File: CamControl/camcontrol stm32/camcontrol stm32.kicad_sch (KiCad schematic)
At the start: 42 parts, among them J1 Power 1, J2 USB_B_Micro, J3 Power 1, J4 Power 1, J5 Power 1, J6 Conn_01x02, J7 Power 1, Q1 AO3401A, Q3 AO3401A, U1 BGS12WN6E6327, U2 BALFHB-WL-02D3, U3 STM32WLE4CCUx, U4 XC6206P332MR, U5 TPS25970LRPWR, U6 TPS25970LRPWR, Y1 32MHz

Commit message: work
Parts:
- removed J2: USB_B_Micro, easyeda2kicad2:MICRO-USB-SMD_U254-051T-4BHJ25-F2S, symbol Connector:USB_B_Micro
- removed J5: Power 1, Connector_Molex:Molex_PicoBlade_53048-0210_1x02_P1.25mm_Horizontal, symbol Connector:Screw_Terminal_01x02
- added C17: 100n, Capacitor_SMD:C_0402_1005Metric, symbol Device:C_Small
- added D2: LED, LED_SMD:LED_0603_1608Metric, symbol Device:LED
- added H1, H2: MountingHole_Pad, MountingHole:MountingHole_2.2mm_M2_DIN965_Pad, symbol Mechanical:MountingHole_Pad
- added J5: Conn_01x06, Connector_PinHeader_1.27mm:PinHeader_1x06_P1.27mm_Vertical, symbol Connector_Generic:Conn_01x06
- added J8: DNP, Connector_PinHeader_2.54mm:PinHeader_1x05_P2.54mm_Vertical, symbol Connector:Conn_01x05_Pin
- added R23, R8: 15k, Resistor_SMD:R_0402_1005Metric, symbol Device:R_Small
- added R24, R9: 51k, Resistor_SMD:R_0402_1005Metric, symbol Device:R_Small
- added R3, R5: 20m, Resistor_SMD:R_0402_1005Metric, symbol Device:R_Small
- added R7: 1k, Resistor_SMD:R_0402_1005Metric, symbol Device:R_Small
- added U7: INA2180, Package_SON:WSON-8-1EP_2x2mm_P0.5mm_EP0.9x1.6mm, symbol .kicad_sym:INA2180
- C15: now not fitted
- C2, C3: footprint Capacitor_SMD:C_0402_1005Metric -> Capacitor_SMD:C_0201_0603Metric
- J1, J3, J4, J7: footprint Connector_Molex:Molex_PicoBlade_53048-0210_1x02_P1.25mm_Horizontal -> Connector_Molex:Molex_PicoBlade_53261-0271_1x02-1MP_P1.25mm_Horizontal
- L1: footprint Inductor_SMD:L_0201_0603Metric -> Inductor_SMD:L_0402_1005Metric
- gave numbers to parts that had none: 1
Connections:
- net PRW1 EN is gone; now on net PRWA EN: U5.1 (EN/UVLO)
- net PWR2 EN is gone; now on net PWRB EN: U6.1 (EN/UVLO)
- net +12V: now also R23.1
- net +12VA: now also R8.1
- net +3V3: now also U1.4 (VDD), C17.1, U7.8 (VS); no longer U3.29 (VDDRF1V55)
- net GND: now also AE1.2 (Shield), J3.1 (Pin_1), J7.1 (Pin_1), U1.2 (GND), C17.2, H1.1, H2.1, J5.3 (Pin_3), J5.6 (Pin_6), J8.4 (Pin_4), J8.5 (Pin_5), R24.2, R7.2, R9.2, U7.4 (GND); no longer J3.2 (Pin_2), J7.2 (Pin_2)
- net PWR A: now also J7.2 (Pin_2), R5.2, U7.2 (IN-1); no longer J7.1 (Pin_1), U5.6 (OUT), U6.6 (OUT)
- net PWR B: now also J3.2 (Pin_2), R3.2, U7.6 (IN-2); no longer J3.1 (Pin_1)
- net VBUS: now also J8.3 (Pin_3)
- net VFBSMPS: now also U3.29 (VDDRF1V55), U3.45 (VFBSMPS)
- net CAM1 TX: now reaches U3.10 (PA3)
- net CAM1 TX: now also J5.2 (Pin_2), J8.2 (Pin_2)
- net BATT SENSE A: now reaches U3.12 (PA4)
- net BATT SENSE A: now also R8.2, R9.1
- net PWRB EN: now reaches U3.13 (PA5)
- net BATT SENSE B: now reaches U3.14 (PA6)
- net BATT SENSE B: now also R23.2, R24.1
- net PRWA EN: now reaches U3.2 (PB4)
- net LED INDICATION: now reaches U3.30 (PB0)
- net LED INDICATION: now also D2.2 (A)
- net CURRENT SENSE B: now reaches U3.34 (PA11)
- net CURRENT SENSE B: now also U7.7 (OUT2)
- net RF CTRL: now reaches U3.38 (PC13)
- net RF CTRL: now also U1.6 (CTRL)
- net CAM2 RX: now reaches U3.4 (PB6)
- net CAM2 RX: now also J5.4 (Pin_4)
- net CAM2 TX: now reaches U3.5 (PB7)
- net CAM2 TX: now also J5.5 (Pin_5)
- net CURRENT SENSE A: now reaches U3.7 (PA0)
- net CURRENT SENSE A: now also U7.1 (OUT1)
- net CAM1 RX: now reaches U3.9 (PA2)
- net CAM1 RX: now also J5.1 (Pin_1), J8.1 (Pin_1)
- new net: D2.1 (K), R7.1
- new net PWR A SENS: R5.1, U5.6 (OUT), U7.3 (IN+1)
- new net PWR B SENS: R3.1, U6.6 (OUT), U7.5 (IN+2)
- no-connect marks 10 -> 27
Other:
- note added: "CURRENT MONITER"
- note added: "DATASHEET"
- note added: "FROM BRIAN"
- note added: "FROM: FOO"
- note added: "MCU"
- note added: "SWITCHES"
- moved on the sheet: C1, C12, C18, J1, J3, J4, J7, R2, R6, U5, U6

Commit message: final version?
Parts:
- removed D4: D_Schottky, Diode_SMD:D_SOD-323F, symbol Device:D_Schottky
- removed H1, H2: MountingHole_Pad, MountingHole:MountingHole_2.2mm_M2_DIN965_Pad, symbol Mechanical:MountingHole_Pad
- removed J8: DNP, Connector_PinHeader_2.54mm:PinHeader_1x05_P2.54mm_Vertical, symbol Connector:Conn_01x05_Pin
- removed Q3: AO3401A, Package_TO_SOT_SMD:SOT-23, symbol Transistor_FET:AO3401A
- removed U4: XC6206P332MR, Package_TO_SOT_SMD:SOT-23-3, symbol .kicad_sym:XC6206P332MR
- added D3: D_Zener, Diode_SMD:D_SOD-523F, symbol Device:D_Zener
- added H1, H2: MountingHole, MountingHole:MountingHole_2.2mm_M2_DIN965, symbol Mechanical:MountingHole
- added J2: Conn_01x04, Connector_PinHeader_2.54mm:PinHeader_1x04_P2.54mm_Vertical, symbol Connector_Generic:Conn_01x04
- added R10: 51k, Resistor_SMD:R_0402_1005Metric, symbol Device:R_Small
- added U4: DS8242, :SOT-23-3_L2.9-W1.6-P1.90-LS2.8-BR, symbol .kicad_sym:DS8242
- J1, J3, J4, J7: footprint Connector_Molex:Molex_PicoBlade_53261-0271_1x02-1MP_P1.25mm_Horizontal -> Connector_Molex:Molex_PicoBlade_53048-0210_1x02_P1.25mm_Horizontal
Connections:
- net +3V3: now also J2.2 (Pin_2), U4.2 (Vout)
- net BATT SENSE A: now also U3.36 (PA13); no longer U3.12 (PA4)
- net BATT SENSE B: now also U3.12 (PA4); no longer U3.14 (PA6)
- net CAM1 RX: now also J2.4 (Pin_4)
- net CAM1 TX: now also J2.3 (Pin_3)
- net CURRENT SENSE B: now also U3.8 (PA1); no longer U3.34 (PA11)
- net GND: now also J2.1 (Pin_1), R10.2, U4.1 (GND); no longer Q1.1 (G)
- net LED INDICATION: now also U3.35 (PA12); no longer U3.30 (PB0)
- net at C5.1, Q1.2 (S): now also D3.1 (K), U4.3 (Vin)
- net at JP1.2 (C): now also Q1.3 (D)
- new net: D3.2 (A), Q1.1 (G), R10.1
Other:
- moved on the sheet: Q1

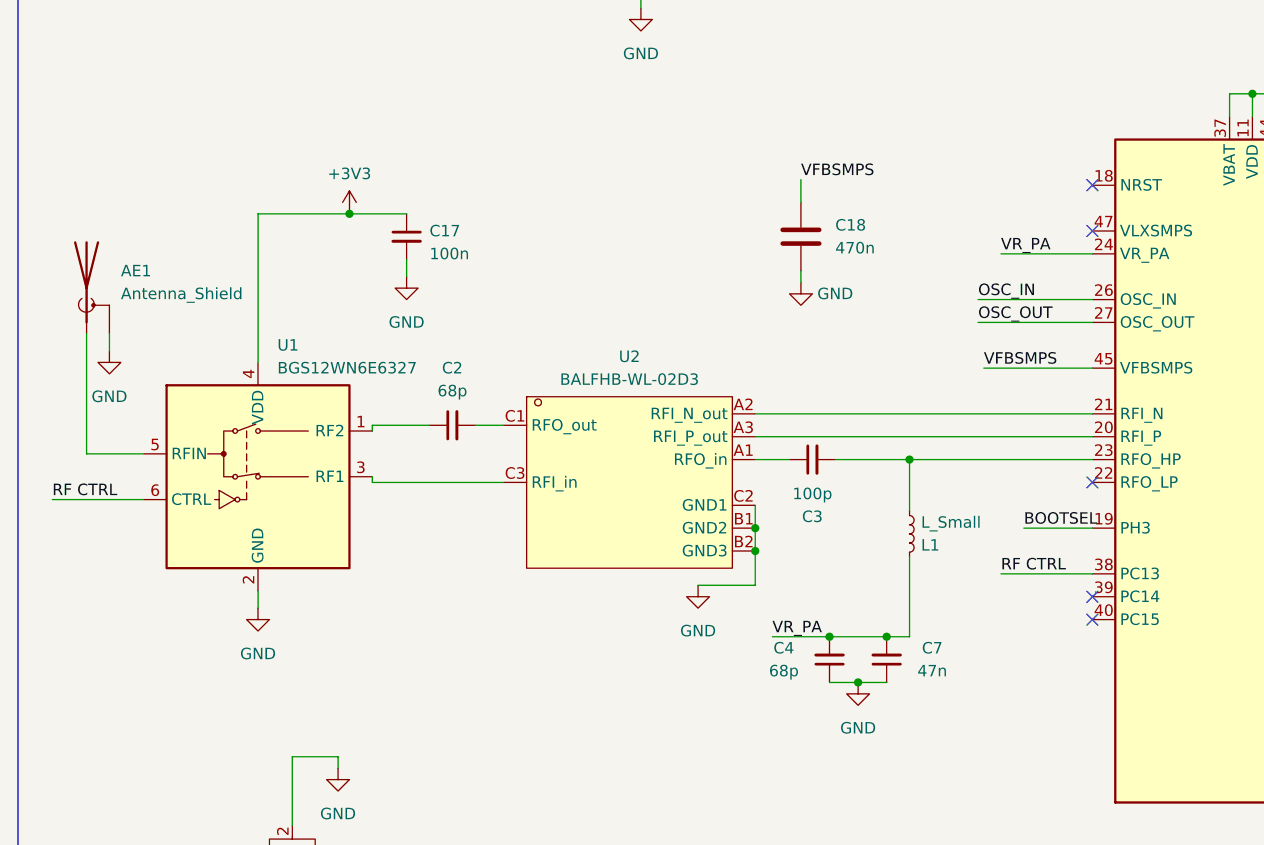
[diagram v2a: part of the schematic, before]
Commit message: rf rework and redrawing
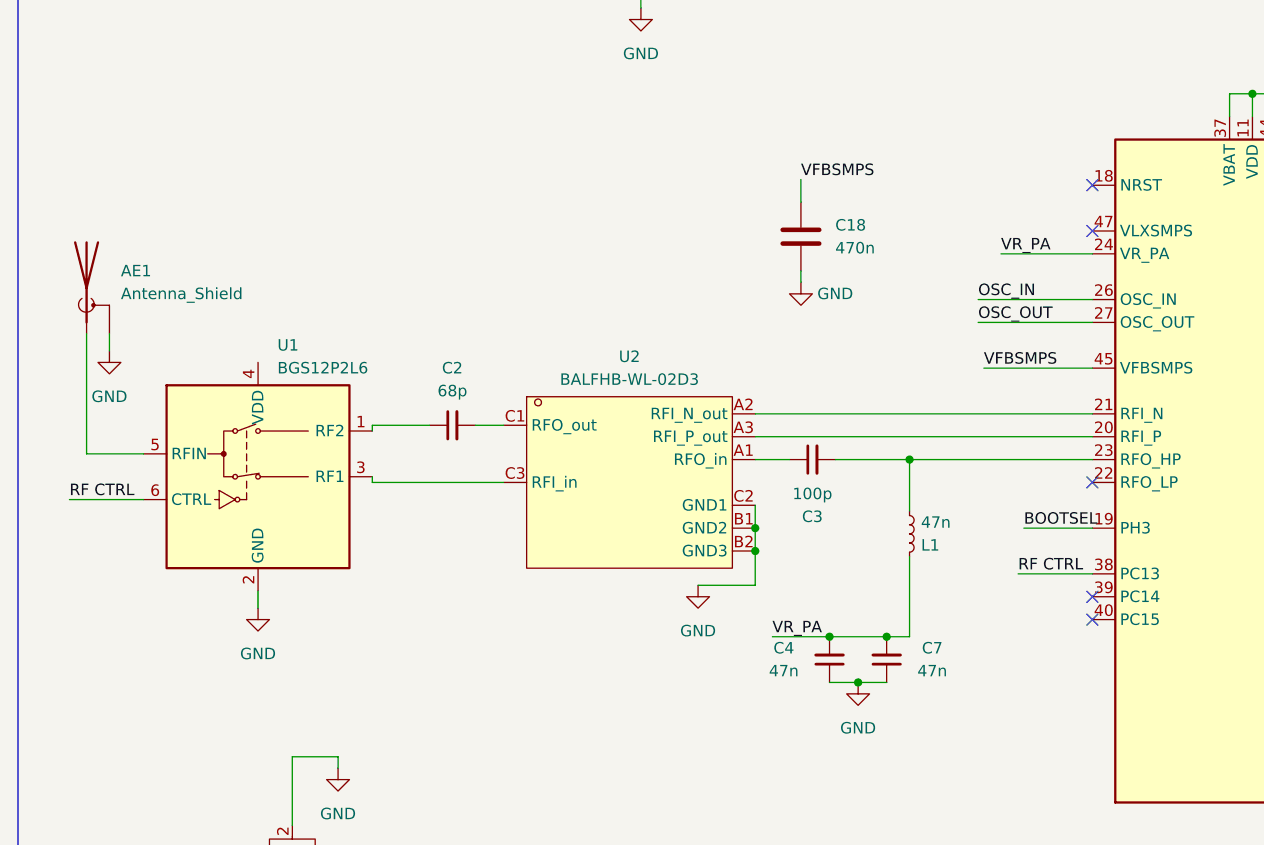
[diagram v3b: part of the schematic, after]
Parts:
- removed C17: 100n, Capacitor_SMD:C_0402_1005Metric, symbol Device:C_Small
- C18: LCSC Part (none) -> C47339
- C4: value 68p -> 47n
- D3: LCSC Part (none) -> C7420320
- L1: value L_Small -> 47n; LCSC Part (none) -> C22334
- R2, R6: LCSC Part (none) -> C25123
- R23, R8: LCSC Part (none) -> C25756
- R4: LCSC Part (none) -> C25779
- U1: value BGS12WN6E6327 -> BGS12P2L6
- U3: LCSC Part (none) -> C2888218
- Y1: LCSC Part (none) -> C383840
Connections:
- net +3V3: no longer U1.4 (VDD)

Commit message: update
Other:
- moved on the sheet: D1, R1
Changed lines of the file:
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@@
 	(rectangle
 		(start 227.965 175.26)
-		(end 283.845 285.115)
+		(end 283.845 284.48)
 		(stroke
 			(width 0)
@@
 	(wire
 		(pts
-			(xy 292.1 181.61) (xy 292.1 180.975)
+			(xy 299.72 186.69) (xy 299.72 186.055)
 		)
 		(stroke
@@
 	(wire
 		(pts
-			(xy 292.1 189.23) (xy 292.1 191.135)
+			(xy 299.72 194.31) (xy 299.72 196.215)
 		)
 		(stroke
@@
 	(wire
 		(pts
-			(xy 292.1 197.485) (xy 292.1 196.215)
+			(xy 299.72 202.565) (xy 299.72 201.295)
 		)
 		(stroke
@@
 	(symbol
 		(lib_id "Device:LED")
-		(at 292.1 185.42 90)
+		(at 299.72 190.5 90)
 		(unit 1)
 		(exclude_from_sim no)
@@
 		(fields_autoplaced yes)
 		(property "Reference" "D1"
-			(at 289.56 188.2776 90)
+			(at 297.18 193.3576 90)
 			(effects
 				(font
@@
 		)
 		(property "Value" "LED"
-			(at 289.56 185.7376 90)
+			(at 297.18 190.8176 90)
 			(effects
 				(font
@@
 		)
 		(property "Footprint" "LED_SMD:LED_0603_1608Metric"
-			(at 292.1 185.42 0)
+			(at 299.72 190.5 0)
 			(effects
 				(font
@@
 		)
 		(property "Datasheet" "~"
-			(at 292.1 185.42 0)
+			(at 299.72 190.5 0)
 			(effects
 				(font
@@
 		)
 		(property "Description" "Light emitting diode"
-			(at 292.1 185.42 0)
+			(at 299.72 190.5 0)
 			(effects
 				(font
@@
 		)
 		(property "LCSC Part" "C89811"
-			(at 292.1 185.42 90)
+			(at 299.72 190.5 90)
 			(effects
 				(font
@@
 		)
 		(property "Sim.Pins" "1=K 2=A"
-			(at 292.1 185.42 0)
+			(at 299.72 190.5 0)
 			(effects
 				(font
@@
 		)
 		(property "Part #" ""
-			(at 292.1 185.42 90)
+			(at 299.72 190.5 90)
 			(effects
 				(font
@@
 	(symbol
 		(lib_id "power:GND")
-		(at 292.1 197.485 0)
+		(at 299.72 202.565 0)
 		(unit 1)
 		(exclude_from_sim no)
@@
 		(fields_autoplaced yes)
 		(property "Reference" "#PWR013"
-			(at 292.1 203.835 0)
+			(at 299.72 208.915 0)
 			(effects
 				(font
@@
 		)
 		(property "Value" "GND"
-			(at 292.1 202.565 0)
+			(at 299.72 207.645 0)
 			(effects
 				(font
@@
 		)
 		(property "Footprint" ""
-			(at 292.1 197.485 0)
+			(at 299.72 202.565 0)
 			(effects
 				(font
@@
 		)
 		(property "Datasheet" ""
-			(at 292.1 197.485 0)
+			(at 299.72 202.565 0)
 			(effects
 				(font
@@
 		)
 		(property "Description" "Power symbol creates a global label with name \"GND\" , ground"
-			(at 292.1 197.485 0)
+			(at 299.72 202.565 0)
 			(effects
 				(font
@@
 	(symbol
 		(lib_id "power:+3V3")
-		(at 292.1 180.975 0)
+		(at 299.72 186.055 0)
 		(unit 1)
 		(exclude_from_sim no)
@@
 		(fields_autoplaced yes)
 		(property "Reference" "#PWR012"
-			(at 292.1 184.785 0)
+			(at 299.72 189.865 0)
 			(effects
 				(font
@@
 		)
 		(property "Value" "+3V3"
-			(at 292.1 177.165 0)
+			(at 299.72 182.245 0)
 			(effects
 				(font
@@
 		)
 		(property "Footprint" ""
-			(at 292.1 180.975 0)
+			(at 299.72 186.055 0)
 			(effects
 				(font
@@
 		)
 		(property "Datasheet" ""
-			(at 292.1 180.975 0)
+			(at 299.72 186.055 0)
 			(effects
 				(font
@@
 		)
 		(property "Description" "Power symbol creates a global label with name \"+3V3\""
-			(at 292.1 180.975 0)
+			(at 299.72 186.055 0)
 			(effects
 				(font
@@
 	(symbol
 		(lib_id "Device:R_Small")
-		(at 292.1 193.675 0)
+		(at 299.72 198.755 0)
 		(unit 1)
 		(exclude_from_sim no)
@@
 		(fields_autoplaced yes)
 		(property "Reference" "R1"
-			(at 290.195 194.31 0)
+			(at 297.815 199.39 0)
 			(effects
 				(font
@@
 		)
 		(property "Value" "1k"
-			(at 290.195 191.77 0)
+			(at 297.815 196.85 0)
 			(effects
 				(font
@@
 		)
 		(property "Footprint" "Resistor_SMD:R_0402_1005Metric"
-			(at 292.1 193.675 0)
+			(at 299.72 198.755 0)
 			(effects
 				(font
@@
 		)
 		(property "Datasheet" "~"
-			(at 292.1 193.675 0)
+			(at 299.72 198.755 0)
 			(effects
 				(font
@@
 		)
 		(property "Description" "Resistor, small symbol"
-			(at 292.1 193.675 0)
+			(at 299.72 198.755 0)
 			(effects
 				(font
@@
 		)
 		(property "LCSC Part" "C11702"
-			(at 292.1 193.675 0)
+			(at 299.72 198.755 0)
 			(effects
 				(font
@@
 		)
 		(property "LCSC_Part" ""
-			(at 292.1 193.675 0)
+			(at 299.72 198.755 0)
 			(effects
 				(font
@@
 		)
 		(property "Part #" ""
-			(at 292.1 193.675 0)
+			(at 299.72 198.755 0)
 			(effects
 				(font

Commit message: hopefully prod version
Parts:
- C2: LCSC Part (none) -> C14441
- C3: LCSC Part (none) -> C1546
- C4, C7: LCSC Part (none) -> C5142571
- R3, R5: value 20m -> 10m; LCSC Part (none) -> C3024467
- U1: LCSC Part (none) -> C3312945
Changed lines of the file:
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@@
 	(wire
 		(pts
-			(xy 123.825 205.74) (xy 131.445 205.74)
+			(xy 122.555 205.74) (xy 131.445 205.74)
 		)
 		(stroke
@@
 	(wire
 		(pts
-			(xy 123.19 210.82) (xy 131.445 210.82)
+			(xy 122.555 210.82) (xy 131.445 210.82)
 		)
 		(stroke
@@
 	)
 	(label "RF CTRL"
-		(at 123.19 210.82 0)
+		(at 122.555 210.82 0)
 		(effects
 			(font
@@
 	)
 	(label "BOOTSEL"
-		(at 123.825 205.74 0)
+		(at 122.555 205.74 0)
 		(effects
 			(font
@@
 			)
 		)
+		(property "LCSC Part" "C5142571"
+			(at 108.585 220.345 0)
+			(effects
+				(font
+					(size 1.27 1.27)
+				)
+				(hide yes)
+			)
+		)
 		(pin "1"
 		)
@@
 			)
 		)
+		(property "LCSC Part" "C5142571"
+			(at 102.235 220.345 0)
+			(effects
+				(font
+					(size 1.27 1.27)
+				)
+				(hide yes)
+			)
+		)
 		(pin "1"
 		)
@@
 			)
 		)
-		(property "Value" "20m"
+		(property "Value" "10m"
 			(at 99.695 43.18 90)
 			(effects
@@
 			)
 		)
+		(property "LCSC Part" "C3024467"
+			(at 99.695 45.72 90)
+			(effects
+				(font
+					(size 1.27 1.27)
+				)
+				(hide yes)
+			)
+		)
 		(pin "2"
 		)
@@
 			)
 		)
+		(property "LCSC Part" "C1546"
+			(at 100.33 198.12 90)
+			(effects
+				(font
+					(size 1.27 1.27)
+				)
+				(hide yes)
+			)
+		)
 		(pin "1"
 		)
@@
 			)
 		)
-		(property "Value" "20m"
+		(property "Value" "10m"
 			(at 204.47 43.18 90)
 			(effects
@@
 			)
 		)
+		(property "LCSC Part" "C3024467"
+			(at 204.47 45.72 90)
+			(effects
+				(font
+					(size 1.27 1.27)
+				)
+				(hide yes)
+			)
+		)
 		(pin "2"
 		)
@@
 			)
 		)
+		(property "LCSC Part" "C3312945"
+			(at 38.735 200.025 0)
+			(effects
+				(font
+					(size 1.27 1.27)
+				)
+				(hide yes)
+			)
+		)
 		(pin "6"
 		)
@@
 			(at 60.325 194.31 90)
 			(effects
+				(font
+					(size 1.27 1.27)
+				)
+				(hide yes)
+			)
+		)
+		(property "LCSC Part" "C14441"
+			(at 60.325 194.31 90)
+			(effects

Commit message: nvm i missed it up
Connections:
- net +3V3: now also U1.4 (VDD)
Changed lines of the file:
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@@
 	(wire
 		(pts
+			(xy 38.735 185.42) (xy 38.735 187.325)
+		)
+		(stroke
+			(width 0)
+			(type default)
+		)
+	)
+	(wire
+		(pts
 			(xy 121.92 120.015) (xy 131.445 120.015)
 		)
@@
 	)
 	(symbol
+		(lib_id "power:+3V3")
+		(at 38.735 185.42 0)
+		(unit 1)
+		(exclude_from_sim no)
+		(in_bom yes)
+		(on_board yes)
+		(dnp no)
+		(fields_autoplaced yes)
+		(property "Reference" "#PWR029"
+			(at 38.735 189.23 0)
+			(effects
+				(font
+					(size 1.27 1.27)
+				)
+				(hide yes)
+			)
+		)
+		(property "Value" "+3V3"
+			(at 38.735 180.975 0)
+			(effects
+				(font
+					(size 1.27 1.27)
+				)
+			)
+		)
+		(property "Footprint" ""
+			(at 38.735 185.42 0)
+			(effects
+				(font
+					(size 1.27 1.27)
+				)
+				(hide yes)
+			)
+		)
+		(property "Datasheet" ""
+			(at 38.735 185.42 0)
+			(effects
+				(font
+					(size 1.27 1.27)
+				)
+				(hide yes)
+			)
+		)
+		(property "Description" "Power symbol creates a global label with name \"+3V3\""
+			(at 38.735 185.42 0)
+			(effects
+				(font
+					(size 1.27 1.27)
+				)
+				(hide yes)
+			)
+		)
+		(pin "1"
+		)
+		(instances
+			(project "camcontrol stm32"
+				(path "/299d0a04-aa0f-4714-a339-a062da4333a5"
+					(reference "#PWR029")
+					(unit 1)
+				)
+			)
+		)
+	)
+	(symbol
 		(lib_id "Device:LED")
 		(at 81.28 135.89 90)
@@
 		(dnp no)
 		(property "Reference" "AE1"
-			(at 23.495 177.1649 0)
+			(at 22.86 174.625 0)
 			(effects
 				(font
@@
 		)
 		(property "Value" "Antenna_Shield"
-			(at 23.495 179.7049 0)
+			(at 22.86 177.165 0)
 			(effects
 				(font

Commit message: things
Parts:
- U7: LCSC Part C83224 -> C2876163
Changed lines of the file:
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@@
 			)
 		)
-		(property "LCSC Part" "C83224"
+		(property "LCSC Part" "C2876163"
 			(at 323.469 99.822 0)
 			(effects
